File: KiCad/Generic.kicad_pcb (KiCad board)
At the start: 2 copper layers, 19 x 29.1 mm, 13 parts, among them J1 Connector, J2 USB-C, J3 VBUS, M1 D24V5F3-NoSHDN, U1 ESP32-WROOM-32, U2 FT230XQ

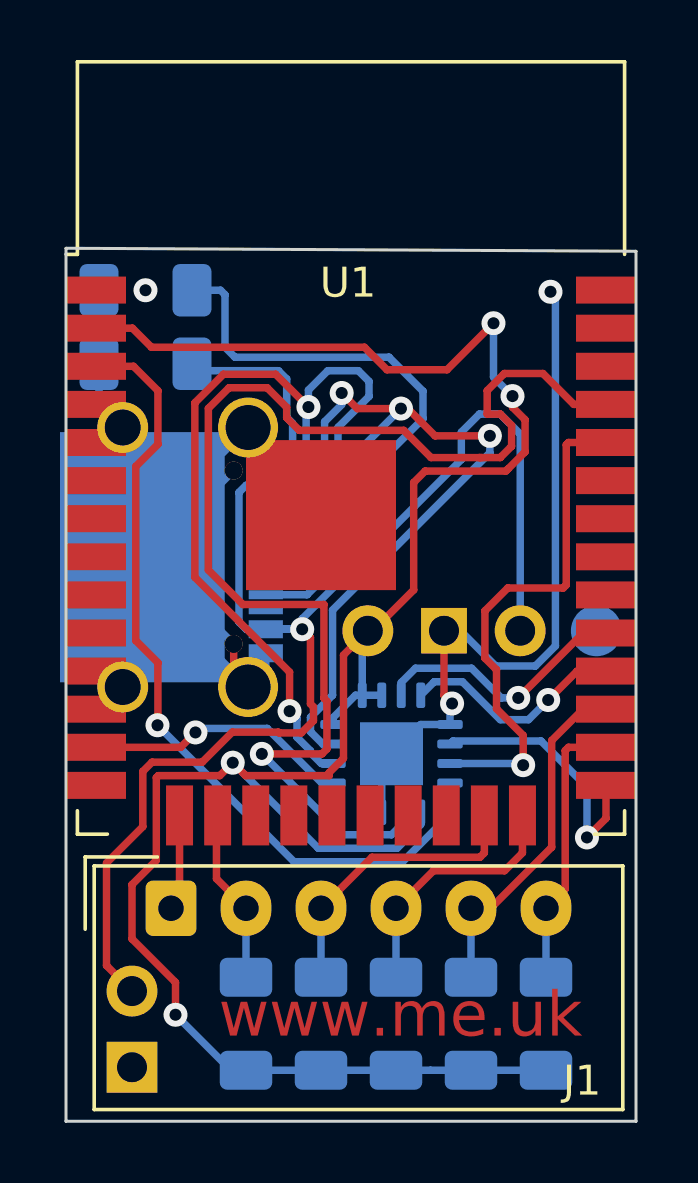
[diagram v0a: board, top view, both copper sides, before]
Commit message: Moved GPI0 to CBUS0
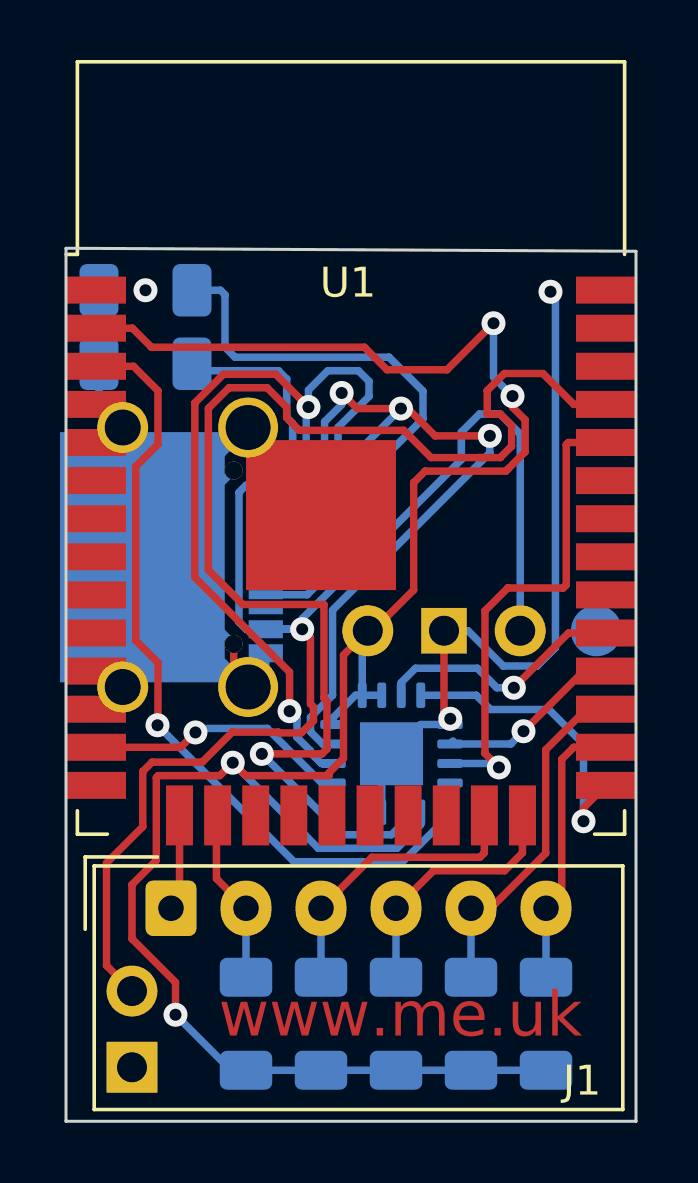
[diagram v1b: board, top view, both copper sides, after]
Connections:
- U1 pad 25: CBUS3 -> CBUS0
- U1 pad 28: CBUS0 -> CBUS3
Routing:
- net CBUS0: track 7.56 -> 10.2 mm
- net CBUS3: track 8.92 -> 6.35 mm
- net I: track 17.2 -> 16.2 mm
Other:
- board text added: "V2"

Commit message: Centred
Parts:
- moved R5 0.27 mm to (128.2, 124.2)
- moved J1 0.27 mm to (115.7, 120.4)
- moved R1 0.27 mm to (118.2, 124.2)
- moved R2 0.27 mm to (120.7, 124.2)
- moved R3 0.27 mm to (123.2, 124.2)
- moved R4 0.27 mm to (125.7, 124.2)
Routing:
- net IO4: track 11.6 -> 12.2 mm
- net IO2: track 9.76 -> 10.4 mm

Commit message: Library update
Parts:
- U2: footprint Package_DFN_QFN:QFN-16-1EP_4x4mm_P0.65mm_EP2.1x2.1mm -> RevK:QFN-16-(hand)-1EP_4x4mm_P0.65mm_EP2.1x2.1mm
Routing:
- net +3V3: track 75.6 -> 81.2 mm
- net EN: track 27.5 -> 32.7 mm
- net O: track 42.0 -> 44.6 mm
- net GND: track 73.1 -> 74.9 mm
- net D+: track 35.3 -> 36.4 mm
- net CBUS0: track 10.2 -> 10.9 mm
- net D-: track 33.9 -> 34.5 mm
- net VBUS: track 44.0 -> 44.5 mm

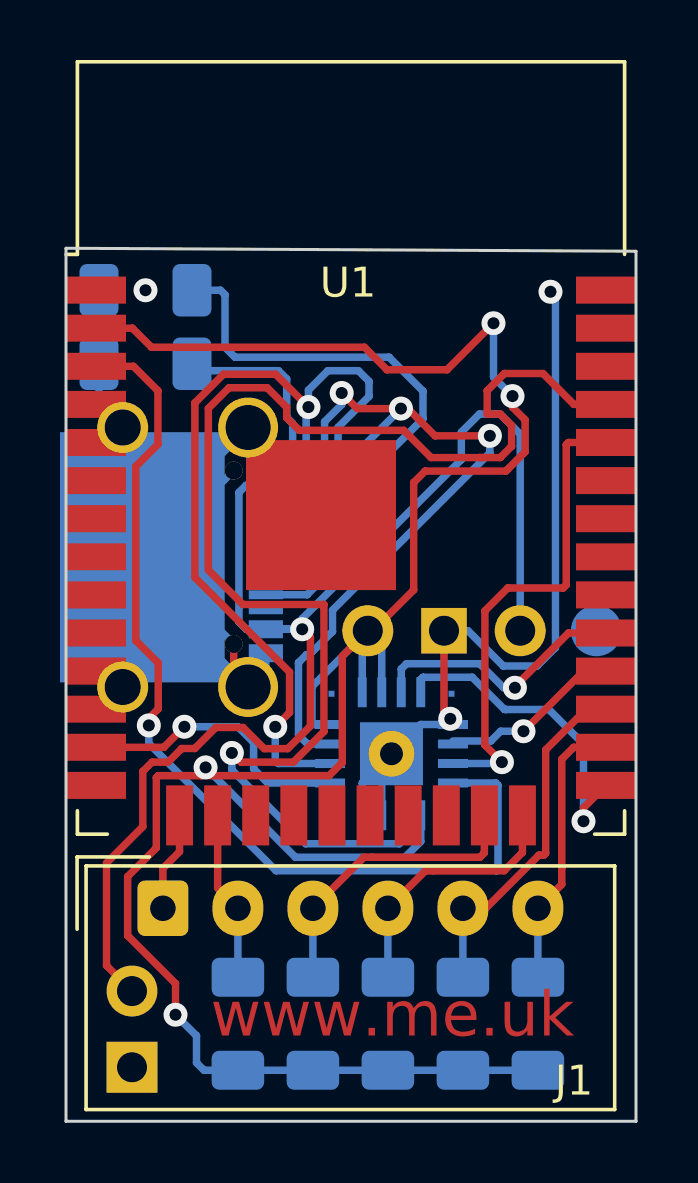
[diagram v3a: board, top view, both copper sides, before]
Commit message: Easier soldering
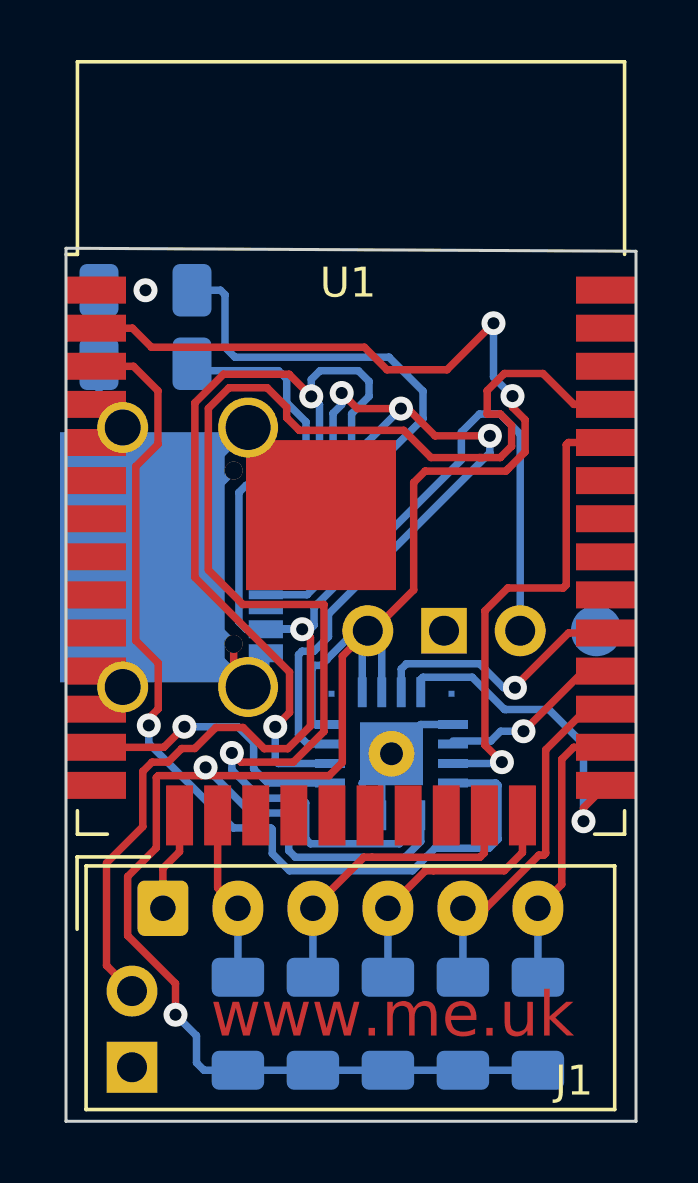
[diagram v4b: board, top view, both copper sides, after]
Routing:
- net GND: track 74.9 -> 55.3 mm, vias 3 -> 1
- net +3V3: track 81.2 -> 82.3 mm
- net O: track 44.6 -> 45.3 mm
